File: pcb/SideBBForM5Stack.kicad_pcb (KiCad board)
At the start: 2 copper layers, 100 x 50 mm, 15 parts, among them J1 Conn_01x14, J2 Conn_01x14, J3 Conn_02x15_Odd_Even, J4 Conn_02x15_Odd_Even

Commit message: Rename project name to SideBBForM5Stack from M5StackSideBB
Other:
- board text added: "SideBBForM5Stack"
- board text added: "https://github.com/asukiaaa/SideBBForM5Stack"
- board text removed: "M5StackSideBB"
- board text removed: "https://github.com/asukiaaa/M5StackSideBB"
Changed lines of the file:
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@@
     (effects (font (size 1 1) (thickness 0.25)))
   )
-  (gr_text "Rev 2019.11" (at 130.0988 87.5792) (layer F.SilkS)
+  (gr_text "Rev 2019.11" (at 133.3488 87.5792) (layer F.SilkS)
     (effects (font (size 1 1) (thickness 0.25)))
   )
-  (gr_text M5StackSideBB (at 113.3348 87.0712) (layer F.SilkS)
+  (gr_text SideBBForM5Stack (at 114.5738 87.0332) (layer F.SilkS)
     (effects (font (size 2 2) (thickness 0.5)))
   )
-  (gr_text https://github.com/asukiaaa/M5StackSideBB (at 173.8884 90.30208) (layer B.SilkS)
+  (gr_text https://github.com/asukiaaa/SideBBForM5Stack (at 178.1738 90.3832) (layer B.SilkS)
     (effects (font (size 1 1.1) (thickness 0.25)) (justify mirror))
   )
-  (gr_text https://github.com/asukiaaa/M5StackSideBB (at 119.4308 89.6112) (layer F.SilkS)
+  (gr_text https://github.com/asukiaaa/SideBBForM5Stack (at 119.4308 89.6112) (layer F.SilkS)
     (effects (font (size 1 1) (thickness 0.25)))
   )
@@
     (effects (font (size 1 1) (thickness 0.25)))
   )
-  (gr_text "Rev 2019.11" (at 160.74136 87.86876) (layer B.SilkS)
+  (gr_text "Rev 2019.11" (at 158.1988 87.8832) (layer B.SilkS)
     (effects (font (size 1.2 1.2) (thickness 0.3)) (justify mirror))
   )
-  (gr_text M5StackSideBB (at 181.52872 87.21852) (layer B.SilkS)
+  (gr_text SideBBForM5Stack (at 181.52872 87.21852) (layer B.SilkS)
     (effects (font (size 2.5 2.5) (thickness 0.625)) (justify mirror))
   )

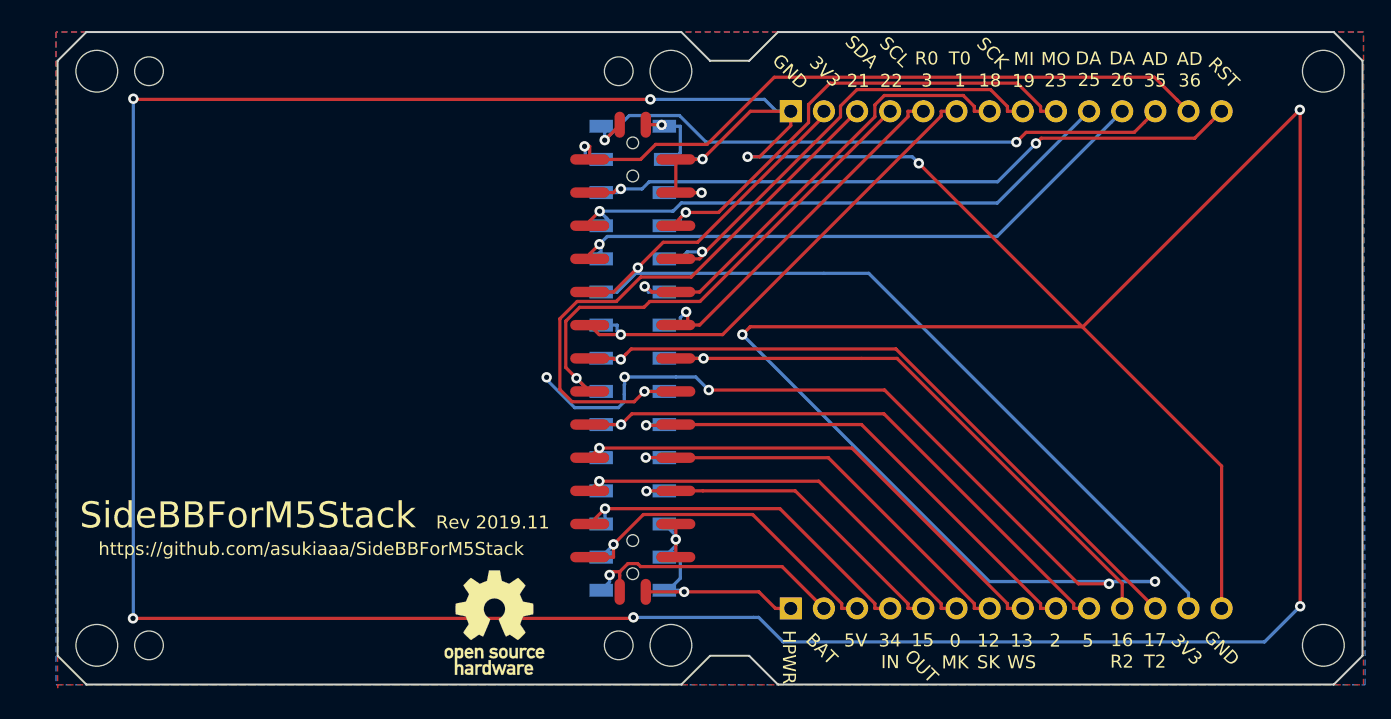
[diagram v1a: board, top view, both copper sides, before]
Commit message: Update size of pads
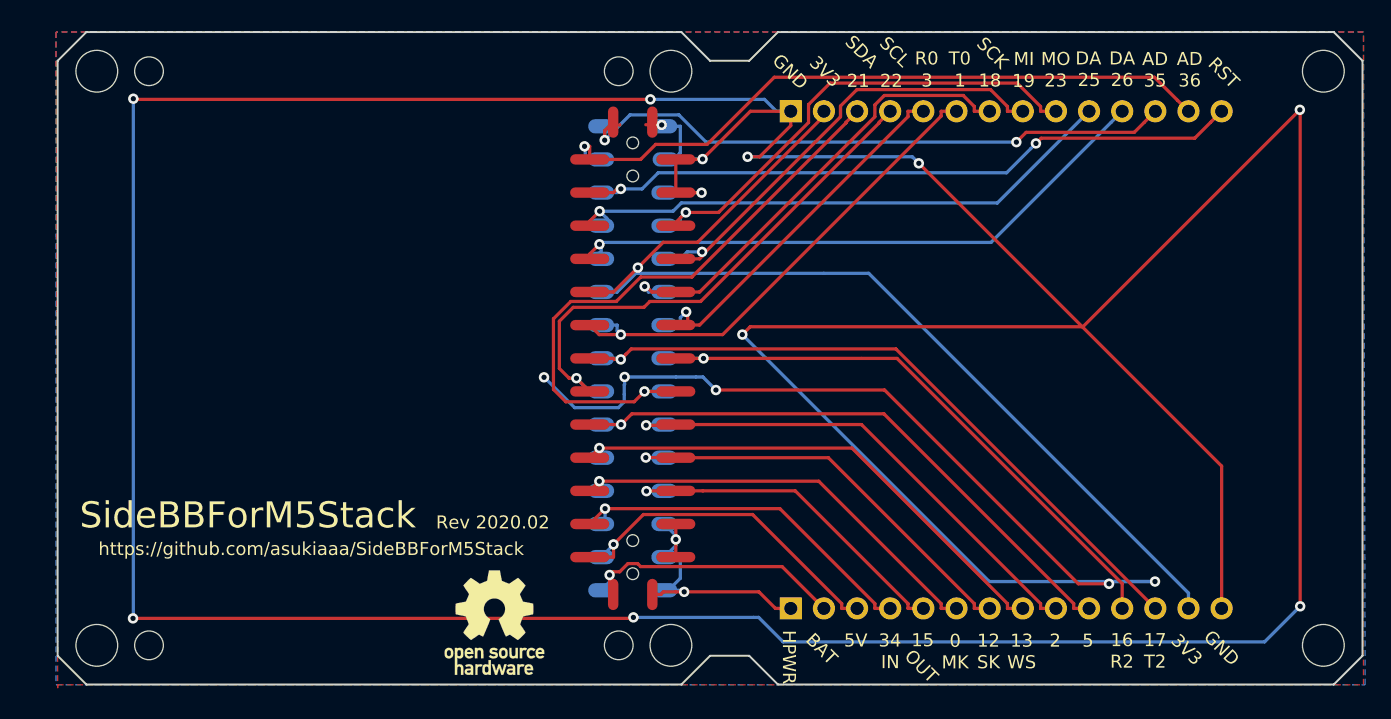
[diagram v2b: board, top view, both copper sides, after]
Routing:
- net G22: track 40.2 -> 41.2 mm
- net G21: track 45.9 -> 46.9 mm
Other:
- board text added: "Rev 2020.02"
- board text removed: "Rev 2019.11"

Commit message: Use 1x15 pinsocket as Rev2021.03
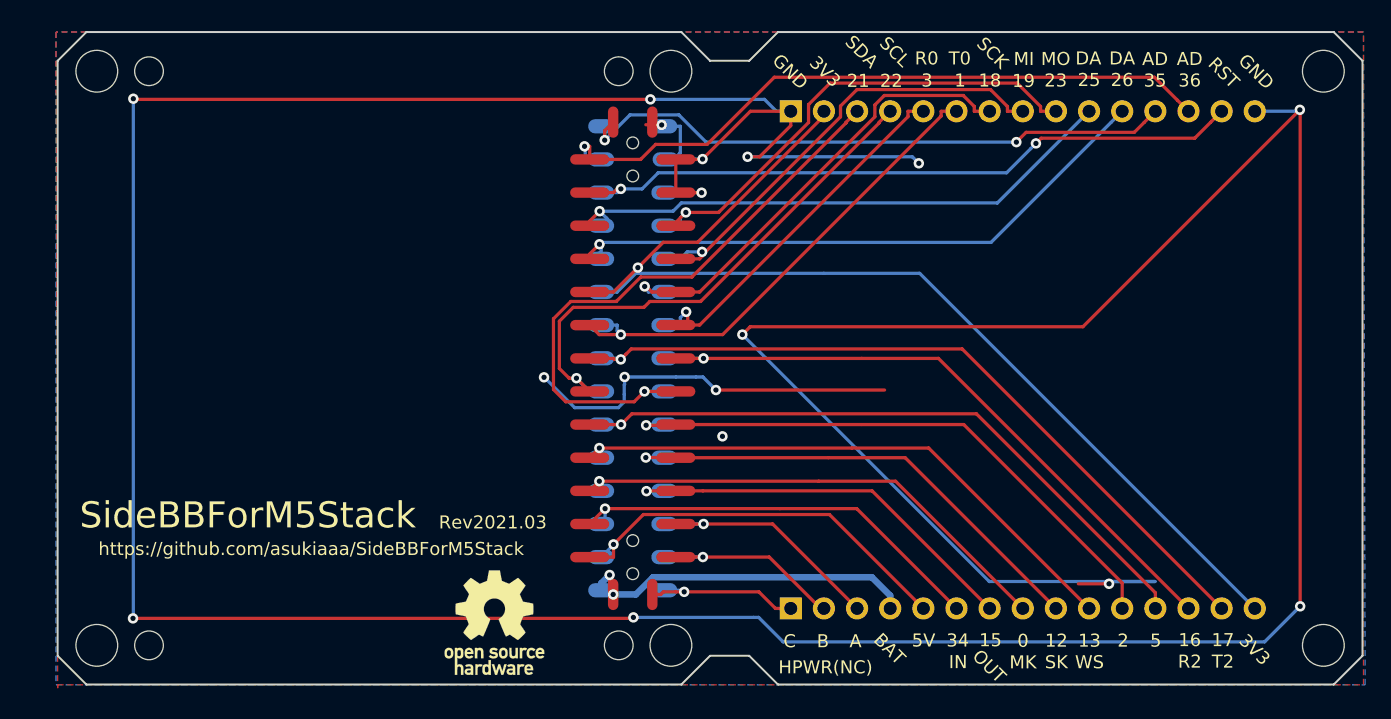
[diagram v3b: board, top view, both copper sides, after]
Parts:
- J1, J2: value Conn_01x14 -> Conn_01x15; footprint footprints:PinSocket_1x14_P2.54mm_Vertical_without_silk -> footprints:PinSocket_1x15_P2.54mm_Vertical_without_silk
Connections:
- J2 pad 1: HPWR -> HPWR_C
- J2 pad 10: G5 -> G13
- J2 pad 11: G16 -> G2
- J2 pad 12: G17 -> G5
- J2 pad 13: +3V3 -> G16
- J2 pad 14: GND -> G17
- J2 pad 2: +BATT -> HPWR_B
- J2 pad 3: +5V -> HPWR_A
- J2 pad 4: G34 -> +BATT
- J2 pad 5: G15 -> +5V
- J2 pad 6: G0 -> G34
- J2 pad 7: G12 -> G15
- J2 pad 8: G13 -> G0
- J2 pad 9: G2 -> G12
- J3 pad 26: HPWR -> HPWR_A
- J3 pad 28: HPWR -> HPWR_B
- J3 pad 30: HPWR -> HPWR_C
- J4 pad 26: HPWR -> HPWR_A
- J4 pad 28: HPWR -> HPWR_B
- J4 pad 30: HPWR -> HPWR_C
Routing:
- net GND: track 455.1 -> 393.8 mm
- net HPWR: track 23.3 -> 0.00 mm, vias 2 -> 0
- net HPWR_A: track 0.00 -> 19.6 mm, vias 0 -> 1
- net HPWR_B: track 0.00 -> 15.9 mm, vias 0 -> 1
- net HPWR_C: track 0.00 -> 12.8 mm, vias 0 -> 1
- net +BATT: track 21.3 -> 27.4 mm, vias 1 -> 2
- net G2: track 38.9 -> 44.9 mm
- net G5: track 46.5 -> 52.1 mm
- net G17: track 53.5 -> 58.6 mm
- net G15: track 26.6 -> 31.4 mm
- net G0: track 33.5 -> 38.3 mm
- net G34: track 28.2 -> 33.1 mm
- net G13: track 39.6 -> 44.5 mm
- net G12: track 32.8 -> 37.6 mm
- net +5V: track 27.0 -> 31.8 mm
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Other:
- board text added: "A"
- board text added: "B"
- board text added: "C"
- board text added: "HPWR(NC)"
- board text added: "Rev2021.03"
- board text removed: "HPWR"
- board text removed: "Rev 2020.02"

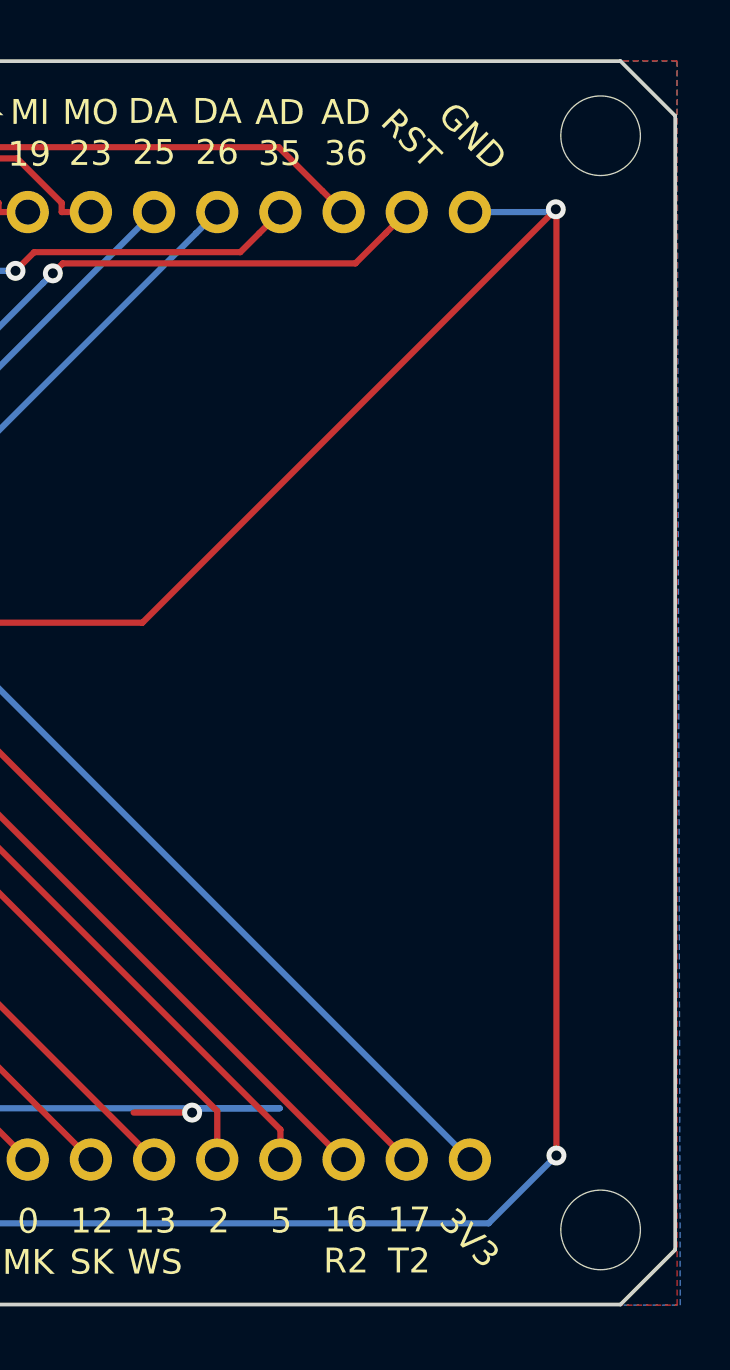
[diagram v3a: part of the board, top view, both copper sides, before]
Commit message: Add label to mension that the labels for Core1
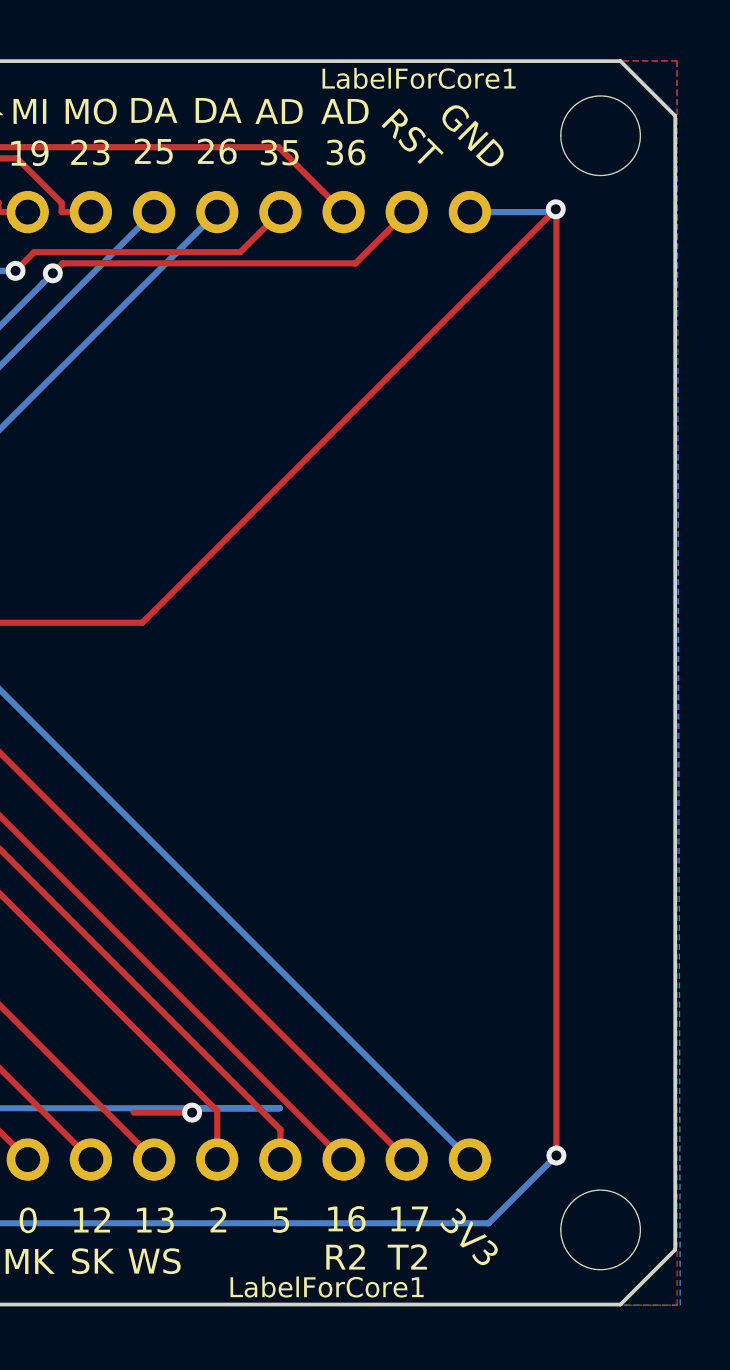
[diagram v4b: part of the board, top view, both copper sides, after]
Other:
- board text added: "LabelForCore1"
